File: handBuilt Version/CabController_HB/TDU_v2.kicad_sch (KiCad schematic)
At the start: 29 parts, among them J28 Conn_02x09_Top_Bottom, J30 SPI, J31 Conn_01x08, J40 Screw_Terminal_01x04, J41 Conn_01x04, J42 Conn_01x04, U10 TPS22960DCNR, U12 TPS22960DCNR

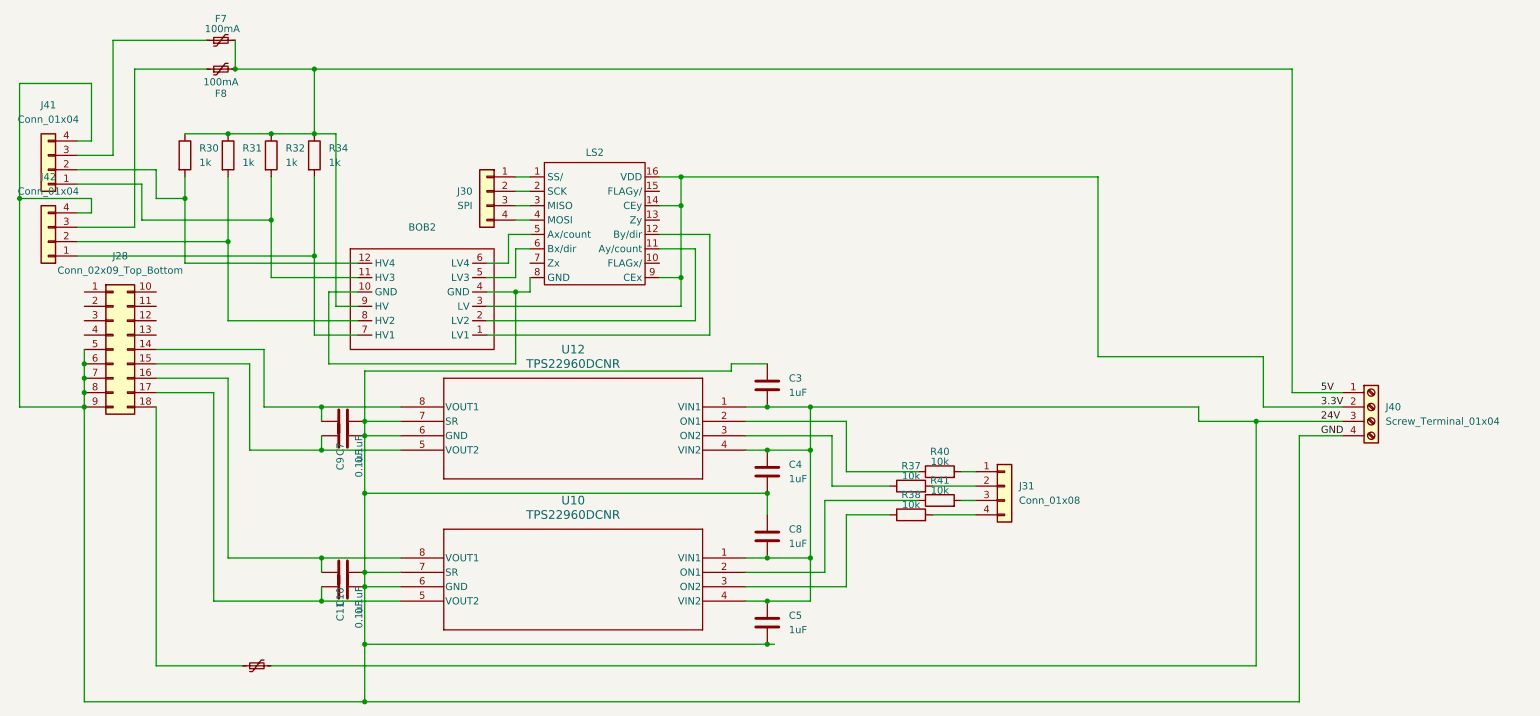
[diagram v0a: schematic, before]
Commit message: Update TDU_v2.kicad_sch
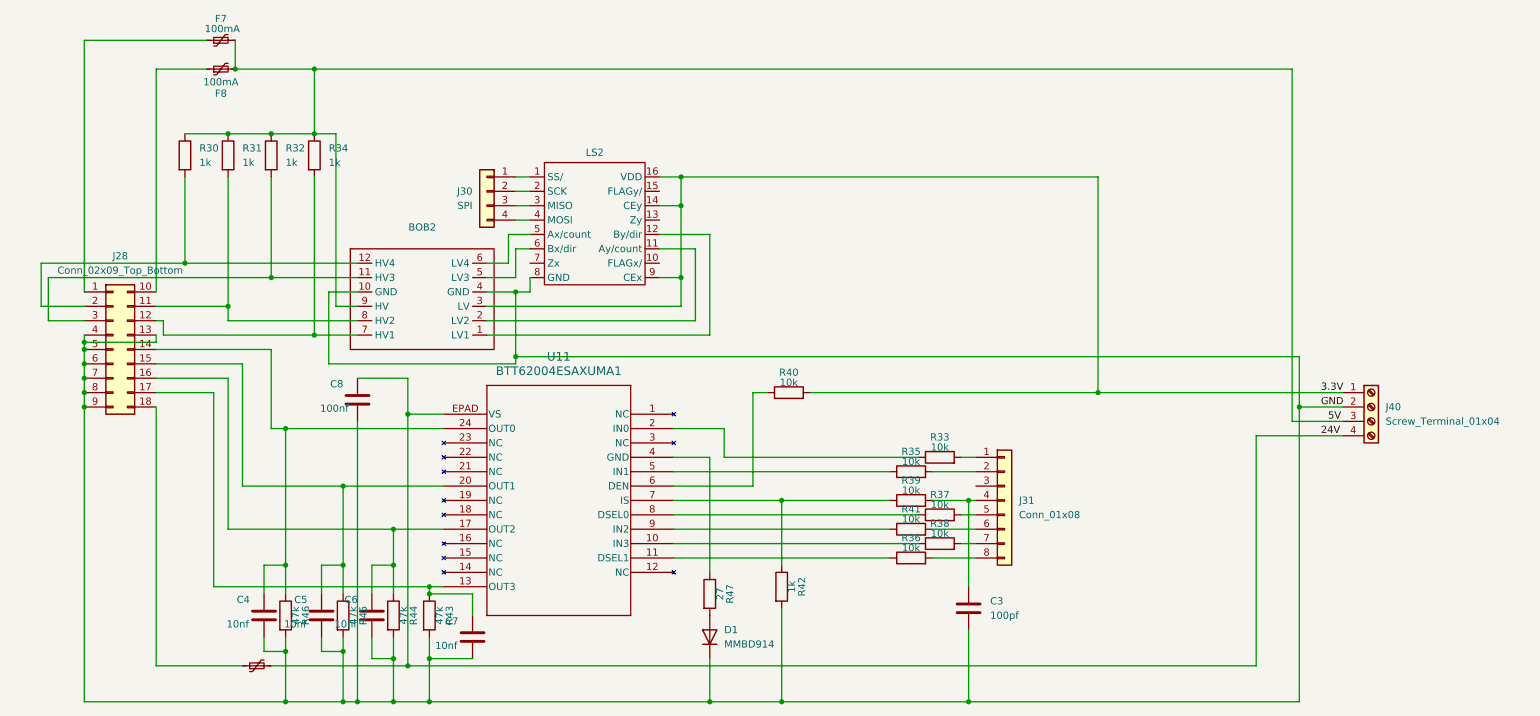
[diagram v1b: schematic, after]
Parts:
- removed C10, C11, C9: 0.1uF, symbol Device:C
- removed J41, J42: Conn_01x04, symbol Connector_Generic:Conn_01x04
- removed U10, U12: TPS22960DCNR, DCN8, symbol HyprLib:TPS22960DCNR
- added C6: 10nf, symbol Device:C
- added D1: MMBD914, Package_TO_SOT_SMD:SOT-23, symbol Diode:BAS21
- added R33, R35, R36, R39: 10k, symbol Device:R
- added R42: 1k, symbol Device:R
- added R43, R44, R45, R46: 47k, symbol Device:R
- added R47: 27, symbol Device:R
- added U11: BTT62004ESAXUMA1, PG-TSDSO-24-21_INF, symbol HyprLib:BTT62004ESAXUMA1
- C3: value 1uF -> 100pf
- C4, C5: value 1uF -> 10nf
- C7: value 0.1uF -> 10nf
- C8: value 1uF -> 100nf
- J31: symbol Connector_Generic:Conn_01x04 -> Connector_Generic:Conn_01x08
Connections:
- net 24V: now also C8.1, J40.4 (Pin_4), U11.EPAD (VS); no longer C3.2, C4.1, C5.1, C8.2, J40.3 (Pin_3)
- net 3.3V: now also J40.1 (Pin_1), R40.2; no longer J40.2 (Pin_2)
- net 5V: now also J40.3 (Pin_3); no longer J40.1 (Pin_1)
- net GND: now also BOB2.10 (GND), BOB2.4 (GND), C3.2, C8.2, J28.13 (Pin_13), J28.4 (Pin_4), J40.2 (Pin_2), LS2.8 (GND), C6.2, D1.3 (K), R42.2, R43.2, R44.2, R45.2, R46.2; no longer C3.1, C8.1, J40.4 (Pin_4)
- net at R40.1: now also U11.6 (DEN)
- net at J31.1 (Pin_1): now also R33.2; no longer R40.2
- net at BOB2.7 (HV1), R34.2: now also J28.12 (Pin_12)
- net at BOB2.8 (HV2), R31.2: now also J28.11 (Pin_11)
- net at F8.1: now also J28.10 (Pin_10)
- net at R37.1: now also U11.8 (DSEL0)
- net at J28.15 (Pin_15): now also C5.1, R45.1, U11.20 (OUT1)
- net at J28.14 (Pin_14): now also C4.1, R46.1, U11.24 (OUT0); no longer C7.1
- net at R38.1: now also U11.10 (IN3)
- net at R38.2: now also J31.7 (Pin_7); no longer J31.4 (Pin_4)
- net at BOB2.11 (HV3), R32.2: now also J28.3 (Pin_3)
- net at BOB2.12 (HV4), R30.2: now also J28.2 (Pin_2)
- net at F7.1: now also J28.1 (Pin_1)
- net at R37.2: now also J31.5 (Pin_5); no longer J31.2 (Pin_2)
- net at J28.16 (Pin_16): now also C6.1, R44.1, U11.17 (OUT2)
- net at J28.17 (Pin_17): now also C7.1, R43.1, U11.13 (OUT3)
- net at J31.3 (Pin_3): no longer R41.2
- net at R41.1: now also U11.9 (IN2)
- new net: R33.1, U11.2 (IN0)
- new net: R36.1, U11.11 (DSEL1)
- new net: R47.1, U11.4 (GND)
- new net: R35.1, U11.5 (IN1)
- new net: R39.1, R42.1, U11.7 (IS)
- new net: J31.2 (Pin_2), R35.2
- new net: C3.1, J31.4 (Pin_4), R39.2
- new net: J31.6 (Pin_6), R41.2
- new net: J31.8 (Pin_8), R36.2
- new net: D1.1 (A), R47.2
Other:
- moved on the sheet: R37, R38, R40, R41
